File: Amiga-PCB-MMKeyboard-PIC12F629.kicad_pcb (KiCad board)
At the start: 2 copper layers, 47.3 x 23.2 mm, 10 parts, among them J11 Amiga BigBox, J12 A500 mainboard, J2 PS/2 keyboard, U1 PIC12F629

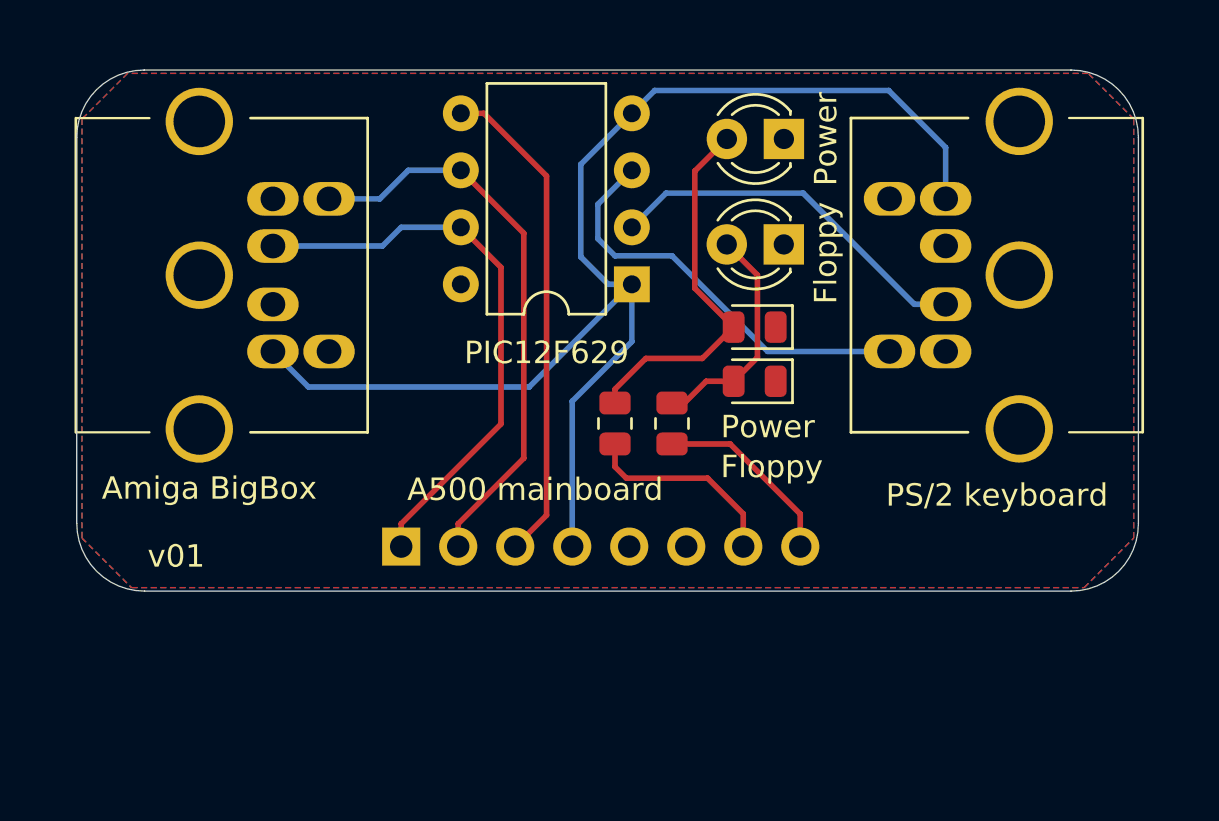
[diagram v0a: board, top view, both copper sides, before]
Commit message: v02
- Update PS/2 socket footprint
- Print "values" on silkscreen
- Add 100 nF for PIC
- Shorten "values"
- Move things to the left for more space and to balance the look
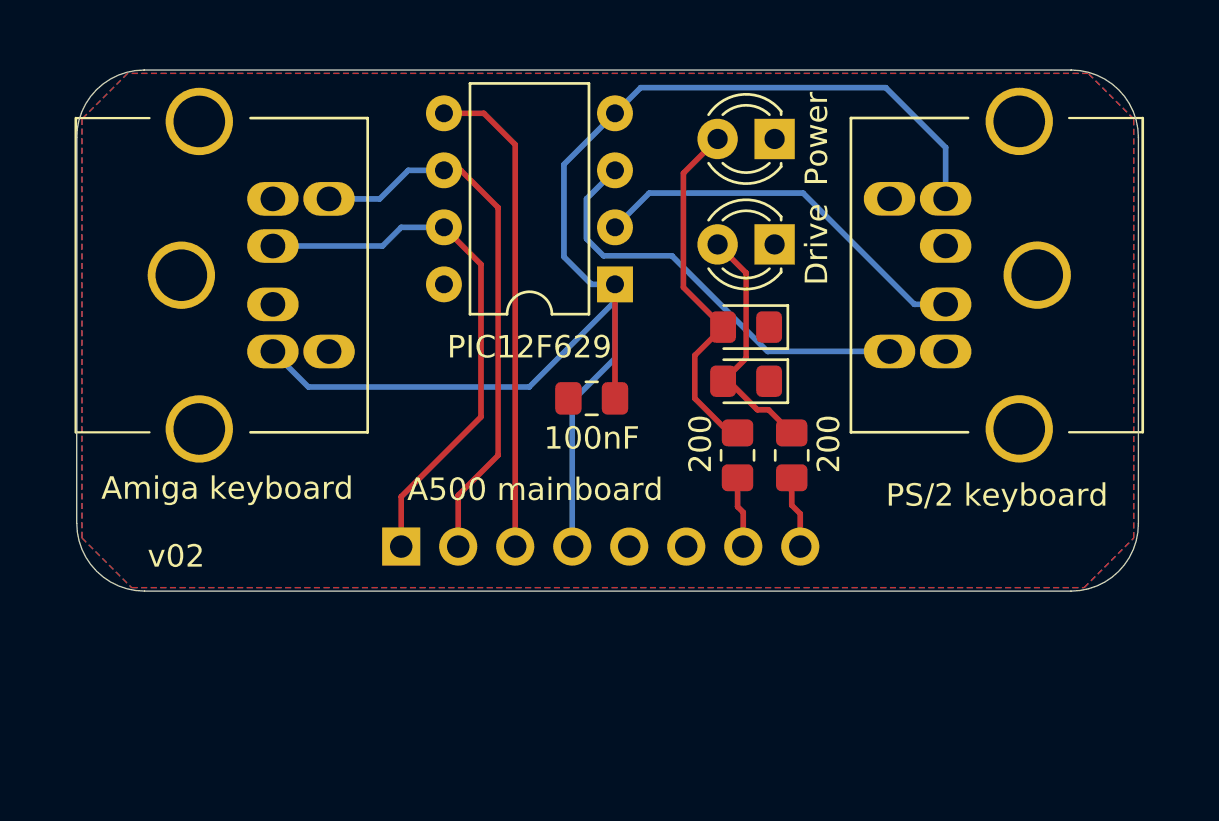
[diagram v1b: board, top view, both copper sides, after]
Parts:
- added C1: 100nF, Capacitor_SMD:C_0805_2012Metric_Pad1.18x1.45mm_HandSolder, F.Cu at (133.6, 98.6)
- D1: value Power -> Power 0805; footprint LED_SMD:LED_0805_2012Metric -> LED_SMD:LED_0805_2012Metric_Pad1.15x1.40mm_HandSolder
- D2: value Floppy -> Drive 0805; footprint LED_SMD:LED_0805_2012Metric -> LED_SMD:LED_0805_2012Metric_Pad1.15x1.40mm_HandSolder
- D4: value Floppy -> Drive
- J11: value Amiga BigBox -> Amiga keyboard
- R1, R2: footprint Resistor_SMD:R_0805_2012Metric -> Resistor_SMD:R_0805_2012Metric_Pad1.20x1.40mm_HandSolder
- moved R1 5.64 mm to (140.1, 101.1)
- moved R2 5.52 mm to (142.5, 101.1)
- moved U1 0.75 mm to (134.6, 93.5)
- moved D3 0.41 mm to (141.7, 87.0)
- moved D4 0.41 mm to (141.7, 91.7)
- moved D1 0.38 mm to (140.5, 95.4)
- moved D2 0.38 mm to (140.5, 97.8)
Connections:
- J11 pad : GND -> (no net)
- J2 pad : GND -> (no net)
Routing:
- net led_power: track 9.06 -> 3.17 mm
- net VCC: track 59.2 -> 64.5 mm
- net led_floppy: track 8.46 -> 3.22 mm
- net amigadat: track 25.5 -> 24.3 mm
- net amigaclock: track 25.5 -> 24.6 mm
- net Net-(D2-A): track 10.2 -> 11.1 mm
- net kdat: track 16.7 -> 17.4 mm
- net Net-(D1-A): track 16.7 -> 16.0 mm
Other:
- board text added: "v02"
- board text removed: "v01"

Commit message: v03: Fix mirrored pin numbering on PS/2 (Mini DIN 6) connectors
The previous versions couldn't actually work due to a mistake in the
Mini DIN 6 connector footprint.
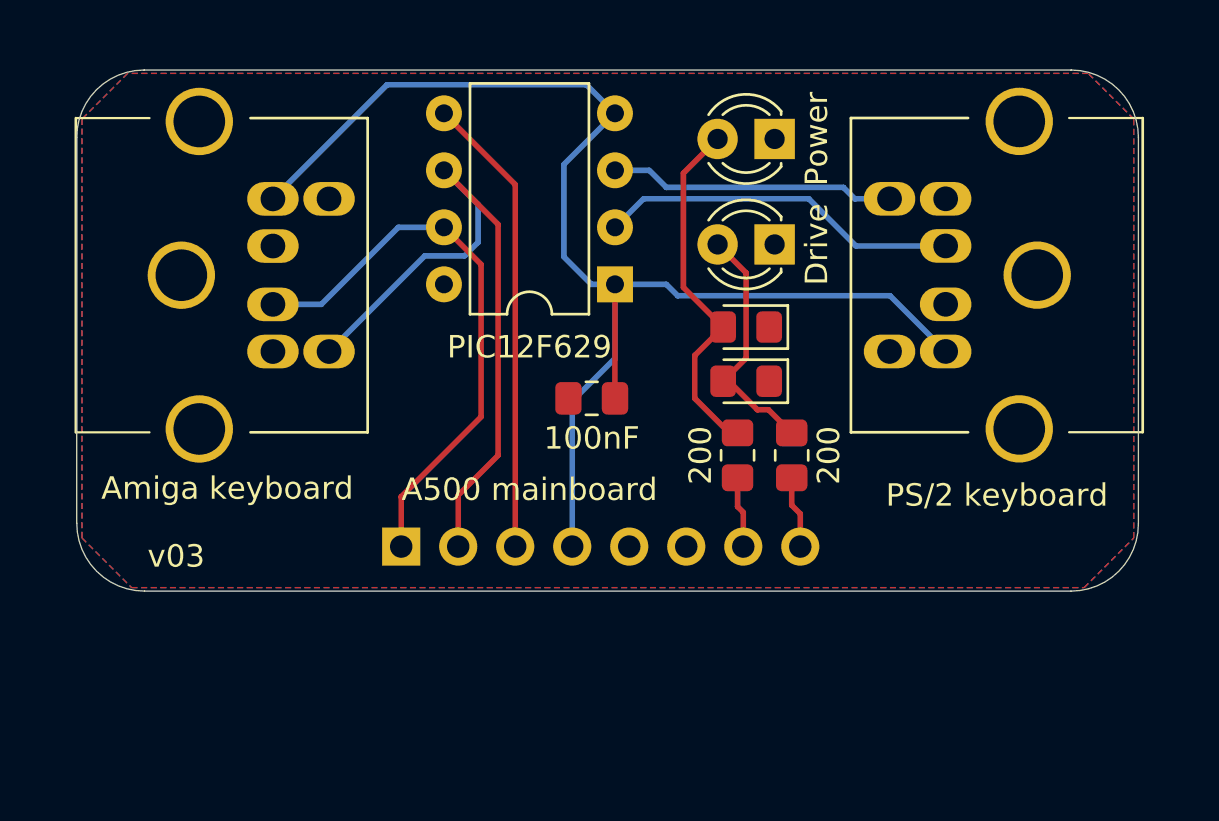
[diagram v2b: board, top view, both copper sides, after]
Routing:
- net amigaclock: track 24.6 -> 31.0 mm
- net kclock: track 19.2 -> 12.8 mm
- net VCC: track 64.5 -> 61.5 mm
- net kdat: track 17.4 -> 16.1 mm
- net amigadat: track 24.3 -> 25.4 mm
- net reset: track 21.7 -> 20.6 mm
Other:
- board text added: "v03"
- board text removed: "v02"

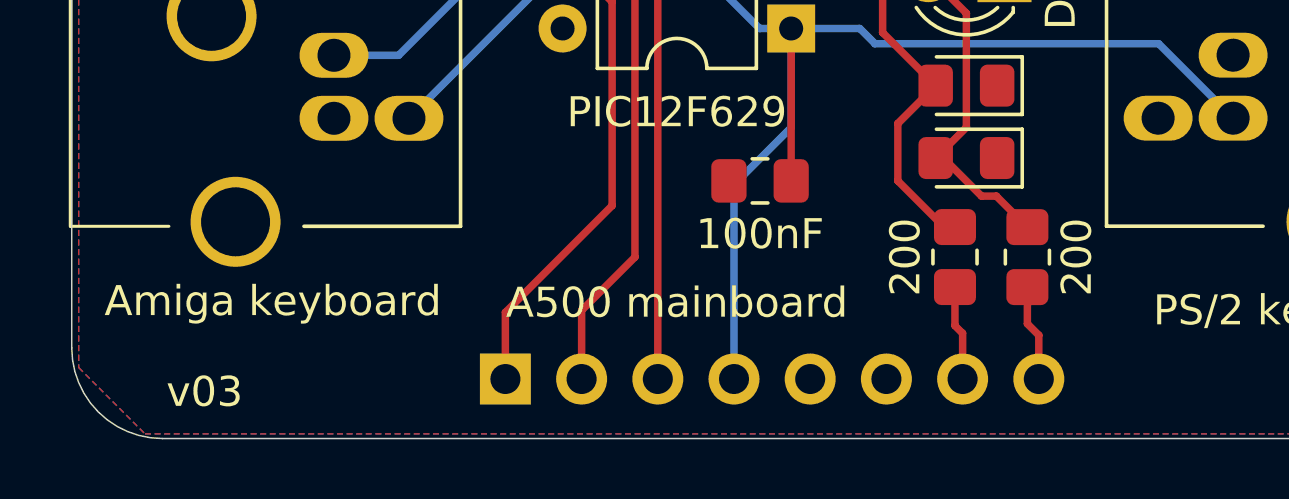
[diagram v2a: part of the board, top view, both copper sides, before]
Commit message: v04: Change resistors to 470 Ohm, late A500 LED colours
200 Ohm are the original value seen on an A500 keyboard, but with modern
0805 LEDs this ends up too bright.

The JLCPCB/LCSC part numbers for the SMD LEDs are now:
 - Power: green
 - Drive: yellow
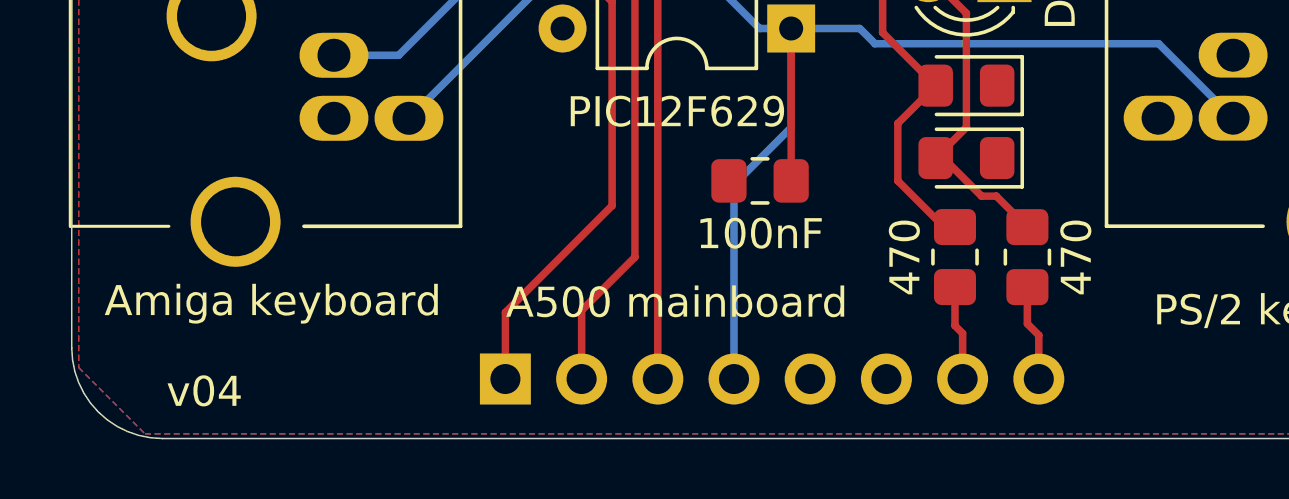
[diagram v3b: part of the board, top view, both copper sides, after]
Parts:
- R1, R2: value 200 -> 470
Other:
- board text added: "v04"
- board text removed: "v03"
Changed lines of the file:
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@@
     (descr "Resistor SMD 0805 (2012 Metric), square (rectangular) end terminal, IPC_7351 nominal with elongated pad for handsoldering. (Body size source: IPC-SM-782 page 72, https://www.pcb-3d.com/wordpress/wp-content/uploads/ipc-sm-782a_amendment_1_and_2.pdf), generated with kicad-footprint-generator")
     (tags "resistor handsolder")
-    (property "JLCPCB" "C17540")
+    (property "JLCPCB" "C17710")
     (property "LCSC" "")
     (property "Sheetfile" "Amiga-PCB-MMKeyboard-PIC12F629.kicad_sch")
@@
         (effects (font (size 1 1) (thickness 0.15)))
     )
-    (fp_text value "200" (at 0 1.651 90) (layer "F.SilkS")
+    (fp_text value "470" (at 0 1.651 90) (layer "F.SilkS")
         (effects (font (size 1 1) (thickness 0.15)))
     )
@@
     (descr "LED SMD 0805 (2012 Metric), square (rectangular) end terminal, IPC_7351 nominal, (Body size source: https://docs.google.com/spreadsheets/d/1BsfQQcO9C6DZCsRaXUlFlo91Tg2WpOkGARC1WS5S8t0/edit?usp=sharing), generated with kicad-footprint-generator")
     (tags "LED handsolder")
-    (property "JLCPCB" "C2297")
+    (property "JLCPCB" "C2296")
     (property "LCSC" "")
     (property "Sheetfile" "Amiga-PCB-MMKeyboard-PIC12F629.kicad_sch")
@@
     (descr "LED SMD 0805 (2012 Metric), square (rectangular) end terminal, IPC_7351 nominal, (Body size source: https://docs.google.com/spreadsheets/d/1BsfQQcO9C6DZCsRaXUlFlo91Tg2WpOkGARC1WS5S8t0/edit?usp=sharing), generated with kicad-footprint-generator")
     (tags "LED handsolder")
-    (property "JLCPCB" "C84256")
+    (property "JLCPCB" "C2297")
     (property "LCSC" "")
     (property "Sheetfile" "Amiga-PCB-MMKeyboard-PIC12F629.kicad_sch")
@@
     (descr "Resistor SMD 0805 (2012 Metric), square (rectangular) end terminal, IPC_7351 nominal with elongated pad for handsoldering. (Body size source: IPC-SM-782 page 72, https://www.pcb-3d.com/wordpress/wp-content/uploads/ipc-sm-782a_amendment_1_and_2.pdf), generated with kicad-footprint-generator")
     (tags "resistor handsolder")
-    (property "JLCPCB" "C17540")
+    (property "JLCPCB" "C17710")
     (property "LCSC" "")
     (property "Sheetfile" "Amiga-PCB-MMKeyboard-PIC12F629.kicad_sch")
@@
         (effects (font (size 1 1) (thickness 0.15)))
     )
-    (fp_text value "200" (at -0.0019 -1.651 90) (layer "F.SilkS")
+    (fp_text value "470" (at -0.0019 -1.651 90) (layer "F.SilkS")
         (effects (font (size 1 1) (thickness 0.15)))
     )
@@
   (gr_arc (start 113.662199 107.14) (mid 111.524899 106.254701) (end 110.6396 104.1174)
     (stroke (width 0.05) (type solid)) (layer "Edge.Cuts"))
-  (gr_text "v03" (at 113.792 106.172) (layer "F.SilkS")
+  (gr_text "v04" (at 113.792 106.172) (layer "F.SilkS")
     (effects (font (size 1 1) (thickness 0.15)) (justify left bottom))
   )

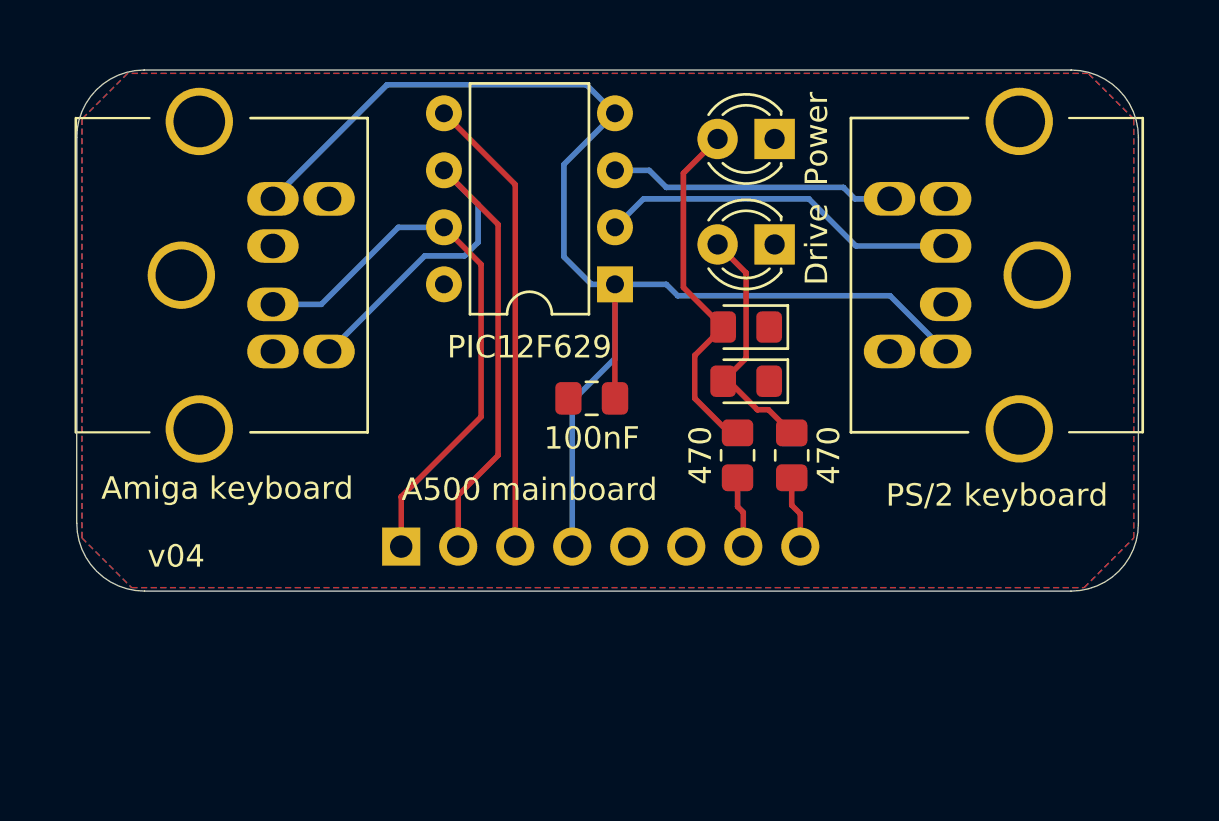
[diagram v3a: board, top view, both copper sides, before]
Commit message: v05: Fix A500 interface, add A500 reset button
The A500 part was untested.
 - data/clock were swapped
 - reset was wrongly connected to the PIC

Added a jumper to reset an A500.
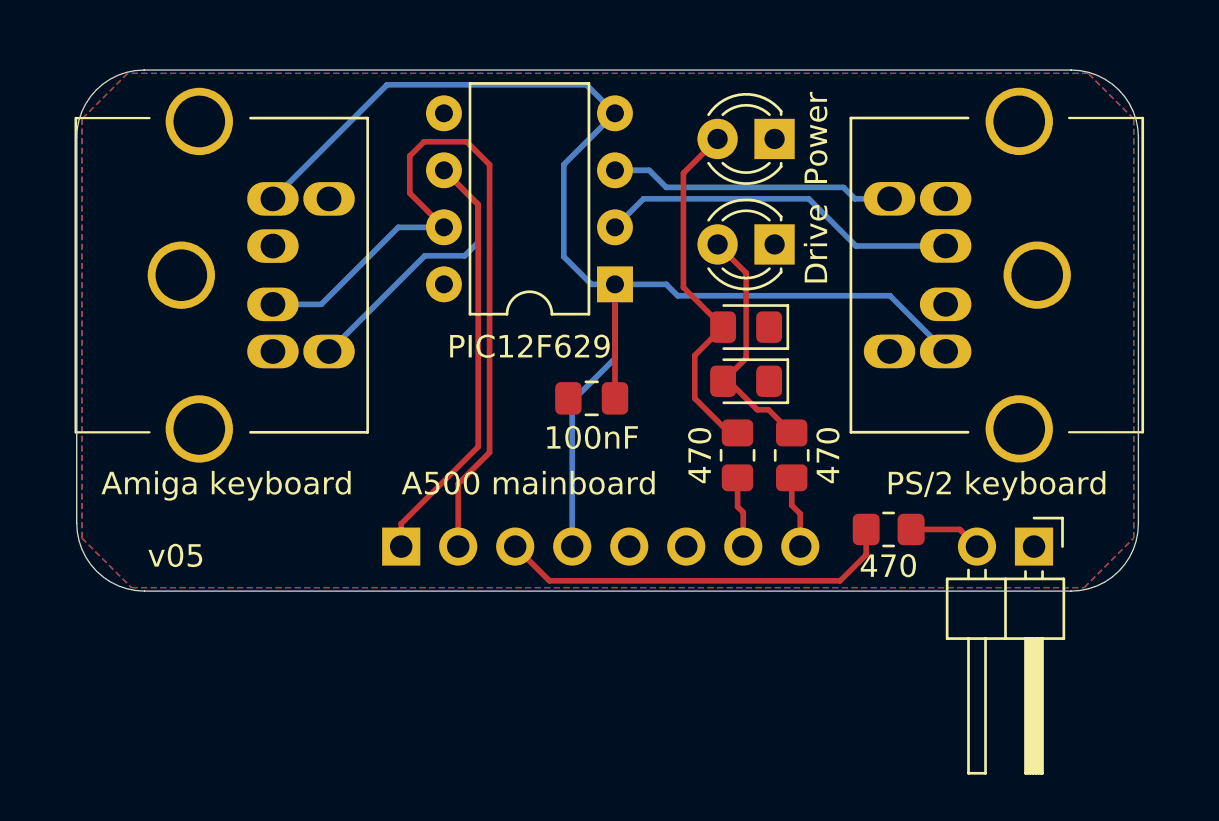
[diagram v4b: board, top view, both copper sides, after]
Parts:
- added R500: 470, Resistor_SMD:R_0805_2012Metric_Pad1.20x1.40mm_HandSolder, F.Cu at (146.8, 104.4)
- added SW500: SW_Push, Connector_PinHeader_2.54mm:PinHeader_1x02_P2.54mm_Horizontal, F.Cu at (153.3, 105.2)
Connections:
- J12 pad 1: amigadat -> amigaclock
- J12 pad 2: amigaclock -> amigadat
- J12 pad 3: reset -> reset500
- U1 pad 5: reset -> reset2000
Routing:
- net reset: track 20.6 -> 0.00 mm
- net reset500: track 0.00 -> 17.9 mm
- net amigadat: track 25.4 -> 34.7 mm
- net Net-(R500-Pad2): track 0.00 -> 3.25 mm
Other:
- board text added: "v05"
- board text removed: "v04"

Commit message: KiCad 9.0 and add local copy of Mini-DIN-6 socket footprint
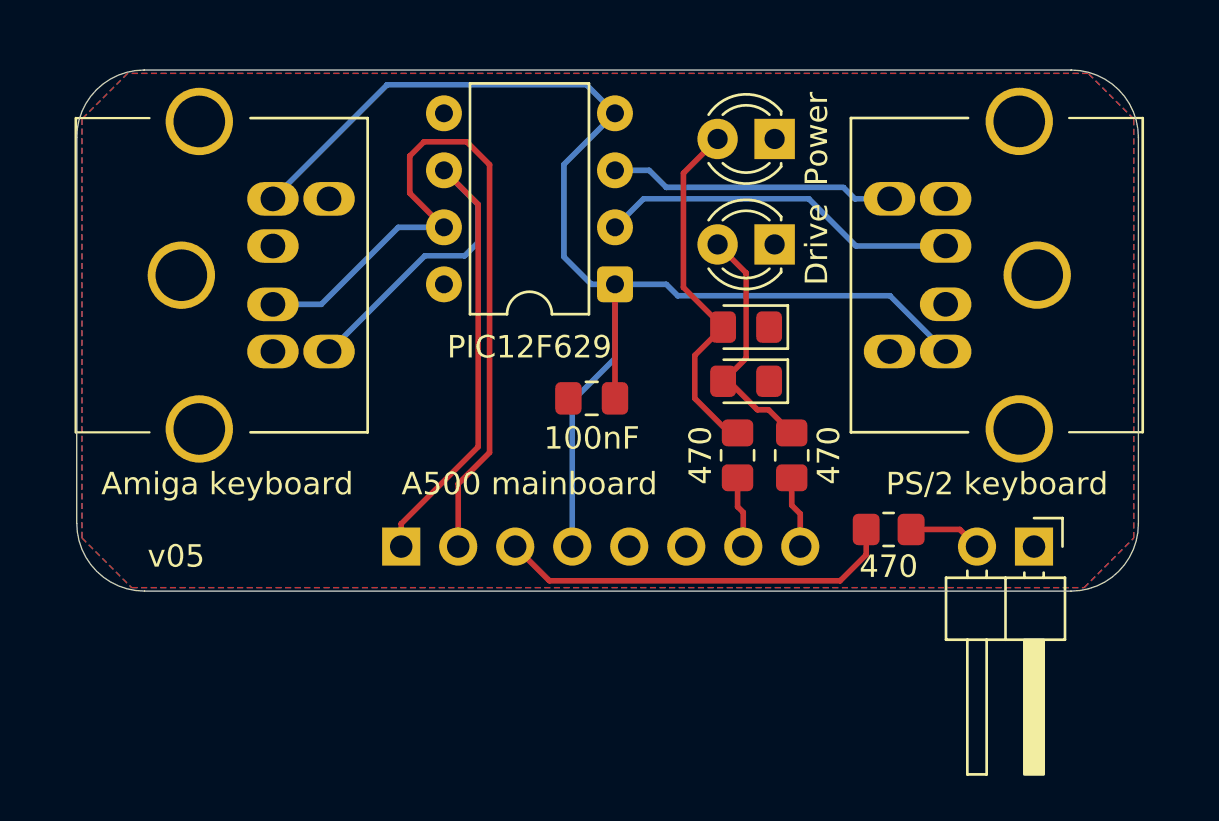
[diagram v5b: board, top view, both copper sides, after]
